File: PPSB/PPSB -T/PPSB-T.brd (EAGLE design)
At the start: 17.8 x 32.7 mm, 8 parts, among them U1 DS18B20

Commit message: Edit PPMB32-E; prepare PPSB-T for sending gerbers to JLCPCB
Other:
- board text added: "GND"
- board text added: "OW"
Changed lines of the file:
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@@
 <drawing>
 <settings>
-<setting alwaysvectorfont="yes"/>
+<setting alwaysvectorfont="no"/>
 <setting verticaltext="up"/>
 </settings>
@@
 <wire x1="17.76" y1="32.69" x2="0" y2="32.69" width="0" layer="20"/>
 <wire x1="0" y1="32.69" x2="0" y2="0" width="0" layer="20"/>
+<text x="7.62" y="0.508" size="0.8128" layer="25">GND</text>
+<text x="2.921" y="0.508" size="0.8128" layer="25">OW</text>
+<text x="2.921" y="30.988" size="0.8128" layer="25">OW</text>
+<text x="7.62" y="30.988" size="0.8128" layer="25">GND</text>
 </plain>
 <attributes>
@@
 </element>
 <element name="OUT" library="#PaJa_konektory" package="ARK500/2" value="ARK500/2" x="6.35" y="26.67" smashed="yes" rot="R180">
-<attribute name="NAME" x="7.775" y="32.068" size="1.4224" layer="25" rot="R180"/>
+<attribute name="NAME" x="15.395" y="32.068" size="1.4224" layer="25" rot="R180"/>
 <attribute name="VALUE" x="11.0593" y="30" size="1.016" layer="27" rot="R180"/>
 </element>

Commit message: Add PanelBoard
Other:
- board text added: "PPSB-T v1.0"
- board text added: "PROTOPlant"
- board text added: "by Petr Stourac"
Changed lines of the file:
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@@
 <drawing>
 <settings>
-<setting alwaysvectorfont="no"/>
+<setting alwaysvectorfont="yes"/>
 <setting verticaltext="up"/>
 </settings>
@@
 <text x="2.921" y="30.988" size="0.8128" layer="25">OW</text>
 <text x="7.62" y="30.988" size="0.8128" layer="25">GND</text>
+<text x="2.159" y="15.748" size="1.778" layer="26" rot="MR270">PPSB-T v1.0</text>
+<text x="17.272" y="15.24" size="1.778" layer="26" rot="MR270">PROTOPlant</text>
+<text x="11.811" y="24.13" size="1.778" layer="26" rot="MR270">by Petr Stourac</text>
 </plain>
 <attributes>

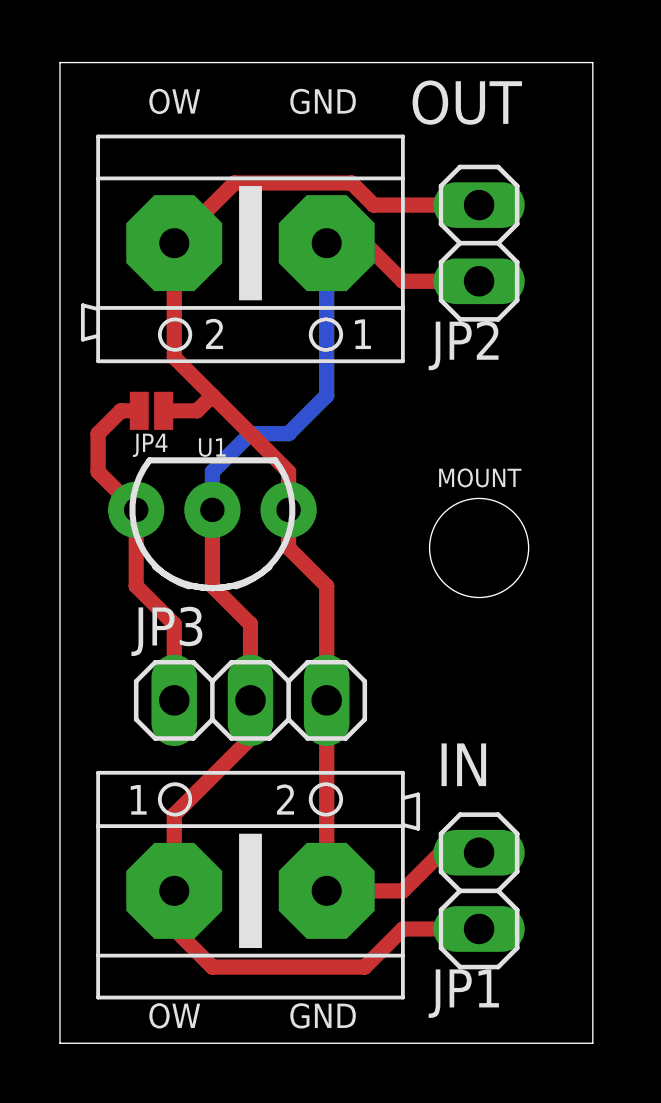
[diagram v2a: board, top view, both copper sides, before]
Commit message: Remove obsolete files, pre-release versions of PPSB-T & PPSB-TH
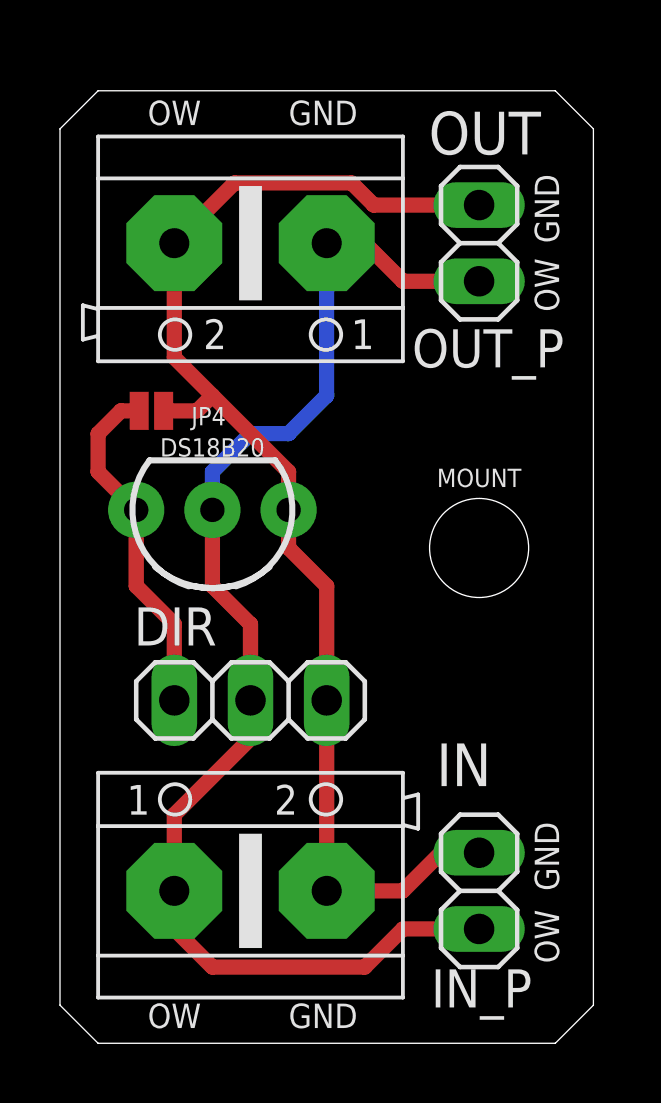
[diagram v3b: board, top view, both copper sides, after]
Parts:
- renumbered JP1 to IN_P, JP2 to OUT_P, JP3 to DIR, U1 to DS18B20
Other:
- board size 17.8 x 32.7 mm -> 17.8 x 31.8 mm
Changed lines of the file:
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@@
 <?xml version="1.0" encoding="utf-8"?>
 <!DOCTYPE eagle SYSTEM "eagle.dtd">
-<eagle version="9.5.2">
+<eagle version="9.6.1">
 <drawing>
 <settings>
@@
 <board>
 <plain>
-<wire x1="0" y1="0" x2="17.76" y2="0" width="0" layer="20"/>
-<wire x1="17.76" y1="0" x2="17.76" y2="32.69" width="0" layer="20"/>
-<wire x1="17.76" y1="32.69" x2="0" y2="32.69" width="0" layer="20"/>
-<wire x1="0" y1="32.69" x2="0" y2="0" width="0" layer="20"/>
 <text x="7.62" y="0.508" size="0.8128" layer="25">GND</text>
 <text x="2.921" y="0.508" size="0.8128" layer="25">OW</text>
-<text x="2.921" y="30.988" size="0.8128" layer="25">OW</text>
-<text x="7.62" y="30.988" size="0.8128" layer="25">GND</text>
+<text x="2.921" y="30.607" size="0.8128" layer="25">OW</text>
+<text x="7.62" y="30.607" size="0.8128" layer="25">GND</text>
 <text x="2.159" y="15.748" size="1.778" layer="26" rot="MR270">PPSB-T v1.0</text>
 <text x="17.272" y="15.24" size="1.778" layer="26" rot="MR270">PROTOPlant</text>
 <text x="11.811" y="24.13" size="1.778" layer="26" rot="MR270">by Petr Stourac</text>
+<text x="16.637" y="2.667" size="0.8128" layer="25" rot="R90">OW</text>
+<text x="16.637" y="5.08" size="0.8128" layer="25" rot="R90">GND</text>
+<text x="16.637" y="24.384" size="0.8128" layer="25" rot="R90">OW</text>
+<text x="16.637" y="26.67" size="0.8128" layer="25" rot="R90">GND</text>
+<wire x1="0" y1="1.27" x2="1.27" y2="0" width="0.0005" layer="20"/>
+<wire x1="1.27" y1="0" x2="16.51" y2="0" width="0.0005" layer="20"/>
+<wire x1="16.51" y1="0" x2="17.78" y2="1.27" width="0.0005" layer="20"/>
+<wire x1="17.78" y1="1.27" x2="17.78" y2="30.48" width="0.0005" layer="20"/>
+<wire x1="17.78" y1="30.48" x2="16.51" y2="31.75" width="0.0005" layer="20"/>
+<wire x1="16.51" y1="31.75" x2="1.27" y2="31.75" width="0.0005" layer="20"/>
+<wire x1="1.27" y1="31.75" x2="0" y2="30.48" width="0.0005" layer="20"/>
+<wire x1="0" y1="30.48" x2="0" y2="1.27" width="0.0005" layer="20"/>
 </plain>
 <attributes>
@@
 <attribute name="VALUE" x="1.6407" y="1.75" size="1.016" layer="27"/>
 </element>
-<element name="JP1" library="pinhead" library_urn="urn:adsk.eagle:library:325" package="1X02" package3d_urn="urn:adsk.eagle:package:22435/2" value="" x="13.97" y="5.08" smashed="yes" rot="R90">
+<element name="IN_P" library="pinhead" library_urn="urn:adsk.eagle:library:325" package="1X02" package3d_urn="urn:adsk.eagle:package:22435/2" value="" x="13.97" y="5.08" smashed="yes" rot="R90">
 <attribute name="NAME" x="12.3698" y="1.1938" size="1.27" layer="25" ratio="10"/>
 <attribute name="POPULARITY" value="98" x="36.83" y="30.48" size="1.778" layer="27" rot="R90" display="off"/>
 <attribute name="VALUE" x="17.145" y="2.54" size="1.27" layer="27" rot="R90"/>
 </element>
-<element name="JP2" library="pinhead" library_urn="urn:adsk.eagle:library:325" package="1X02" package3d_urn="urn:adsk.eagle:package:22435/2" value="" x="13.97" y="26.67" smashed="yes" rot="R90">
-<attribute name="NAME" x="12.3698" y="22.7838" size="1.27" layer="25" ratio="10"/>
+<element name="OUT_P" library="pinhead" library_urn="urn:adsk.eagle:library:325" package="1X02" package3d_urn="urn:adsk.eagle:package:22435/2" value="" x="13.97" y="26.67" smashed="yes" rot="R90">
+<attribute name="NAME" x="11.7348" y="22.5298" size="1.27" layer="25" ratio="10"/>
 <attribute name="POPULARITY" value="98" x="43.18" y="43.18" size="1.778" layer="27" rot="R90" display="off"/>
 <attribute name="VALUE" x="17.145" y="24.13" size="1.27" layer="27" rot="R90"/>
 </element>
-<element name="JP3" library="pinhead" library_urn="urn:adsk.eagle:library:325" package="1X03" package3d_urn="urn:adsk.eagle:package:22458/2" value="" x="6.35" y="11.43" smashed="yes">
+<element name="DIR" library="pinhead" library_urn="urn:adsk.eagle:library:325" package="1X03" package3d_urn="urn:adsk.eagle:package:22458/2" value="" x="6.35" y="11.43" smashed="yes">
 <attribute name="NAME" x="2.4638" y="13.2588" size="1.27" layer="25" ratio="10"/>
 <attribute name="POPULARITY" value="92" x="24.13" y="-11.43" size="1.778" layer="27" display="off"/>
@@
 </element>
 <element name="OUT" library="#PaJa_konektory" package="ARK500/2" value="ARK500/2" x="6.35" y="26.67" smashed="yes" rot="R180">
-<attribute name="NAME" x="15.395" y="32.068" size="1.4224" layer="25" rot="R180"/>
+<attribute name="NAME" x="16.03" y="31.052" size="1.4224" layer="25" rot="R180"/>
 <attribute name="VALUE" x="11.0593" y="30" size="1.016" layer="27" rot="R180"/>
 </element>
-<element name="U1" library="SparkFun-Sensors" package="TO-92-AMMO" value="DS18B20" x="5.08" y="17.78" smashed="yes" rot="R180">
+<element name="DS18B20" library="SparkFun-Sensors" package="TO-92-AMMO" value="DS18B20" x="5.08" y="17.78" smashed="yes" rot="R180">
 <attribute name="NAME" x="5.08" y="19.558" size="0.6096" layer="25" font="vector" ratio="20" align="bottom-center"/>
 <attribute name="STORE_ID" value="SEN-00245" x="-22.86" y="31.75" size="1.778" layer="27" rot="R180" display="off"/>
@@
 </element>
 <element name="JP4" library="SparkFun-Jumpers" package="SMT-JUMPER_2_NO_NO-SILK" package3d_urn="urn:adsk.eagle:package:39277/1" value="NO_JP" x="3.048" y="21.082" smashed="yes" rot="R180">
-<attribute name="NAME" x="3.048" y="20.32" size="0.6096" layer="25" font="vector" ratio="20" rot="R180" align="bottom-center"/>
+<attribute name="NAME" x="4.953" y="21.209" size="0.6096" layer="25" font="vector" ratio="20" rot="R180" align="bottom-center"/>
 <attribute name="VALUE" x="3.048" y="22.225" size="0.6096" layer="27" font="vector" ratio="20" rot="R180" align="top-center"/>
 </element>
@@
 <signals>
 <signal name="GND">
-<contactref element="U1" pad="1"/>
-<contactref element="JP3" pad="3"/>
+<contactref element="DS18B20" pad="1"/>
+<contactref element="DIR" pad="3"/>
 <contactref element="OUT" pad="2"/>
-<contactref element="JP2" pad="2"/>
+<contactref element="OUT_P" pad="2"/>
 <contactref element="IN" pad="2"/>
-<contactref element="JP1" pad="2"/>
+<contactref element="IN_P" pad="2"/>
 <wire x1="8.89" y1="11.43" x2="8.89" y2="5.08" width="0.508" layer="1"/>
 <contactref element="JP4" pad="1"/>
@@
 </signal>
 <signal name="ONEWIRE_BUS">
-<contactref element="U1" pad="2"/>
-<contactref element="JP3" pad="2"/>
+<contactref element="DS18B20" pad="2"/>
+<contactref element="DIR" pad="2"/>
 <contactref element="IN" pad="1"/>
-<contactref element="JP1" pad="1"/>
+<contactref element="IN_P" pad="1"/>
 <contactref element="OUT" pad="1"/>
-<contactref element="JP2" pad="1"/>
+<contactref element="OUT_P" pad="1"/>
 <wire x1="6.35" y1="11.43" x2="6.35" y2="10.16" width="0.508" layer="1"/>
 <wire x1="3.81" y1="7.62" x2="3.81" y2="5.08" width="0.508" layer="1"/>
@@
 </signal>
 <signal name="N$1">
-<contactref element="JP3" pad="1"/>
-<contactref element="U1" pad="3"/>
+<contactref element="DIR" pad="1"/>
+<contactref element="DS18B20" pad="3"/>
 <contactref element="JP4" pad="2"/>
 <wire x1="3.81" y1="11.43" x2="3.81" y2="13.97" width="0.508" layer="1"/>
